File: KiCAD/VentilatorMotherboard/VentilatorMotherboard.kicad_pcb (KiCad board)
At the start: 2 copper layers, 139.7 x 151.1 mm, 31 parts

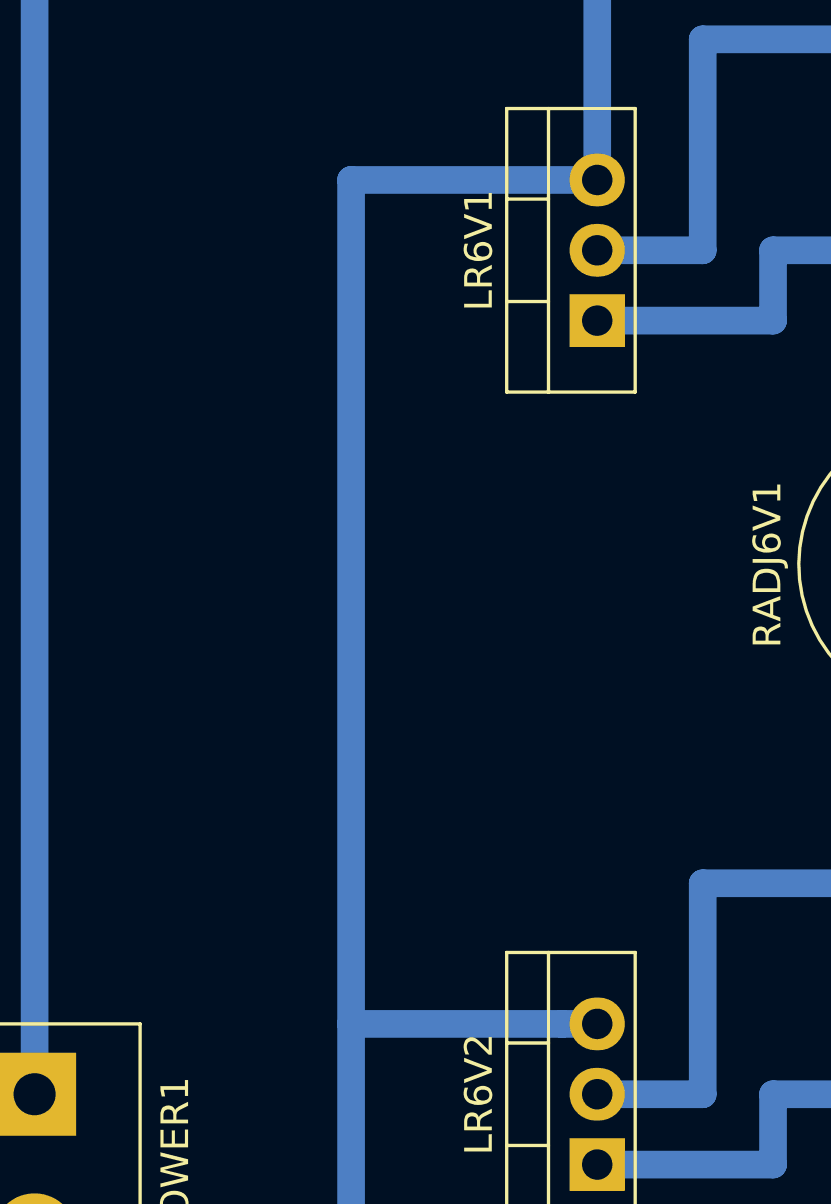
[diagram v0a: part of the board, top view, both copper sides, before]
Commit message: Add power switch to PCB; add some text annotations
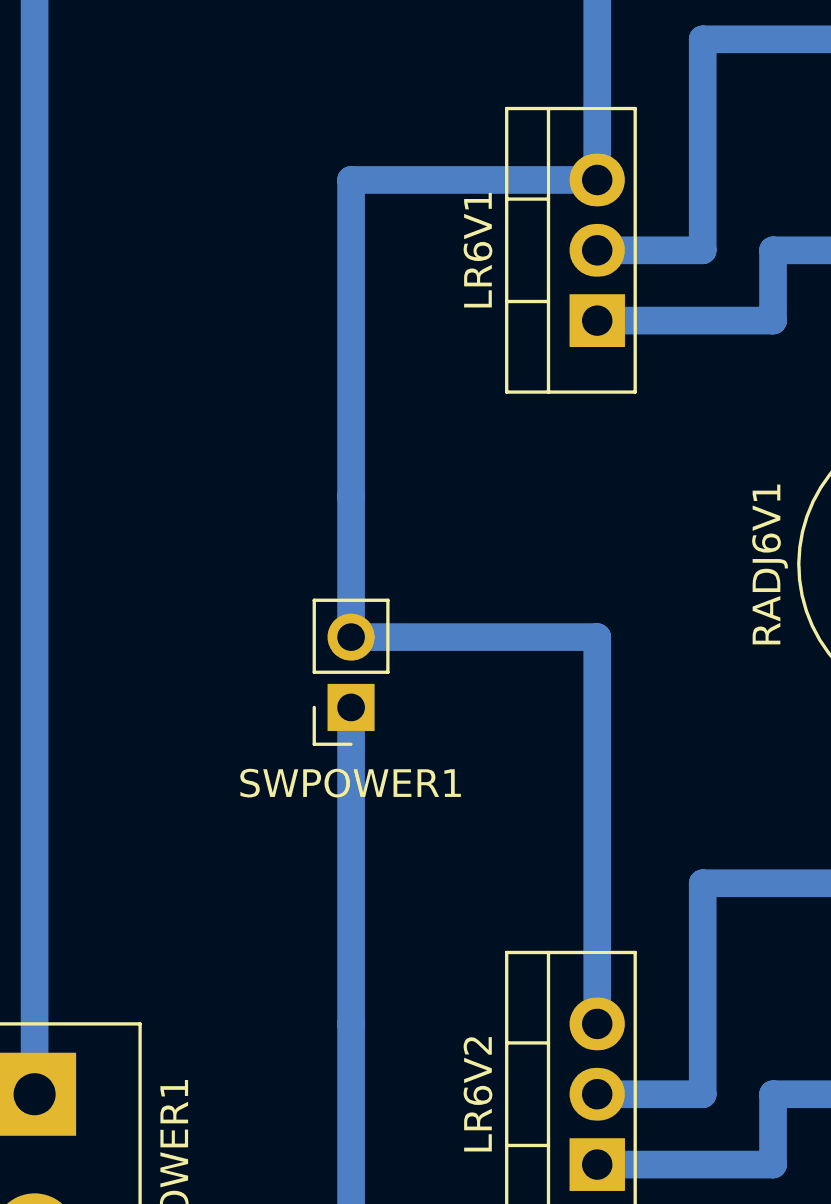
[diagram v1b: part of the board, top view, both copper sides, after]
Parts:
- added SWPOWER1: SW_SPST, Connector_PinSocket_2.54mm:PinSocket_1x02_P2.54mm_Vertical, F.Cu at (59.7, 59.7)
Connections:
- LR5V1 pad 1: Net-(JPOWER1-Pad2) -> Net-(LR5V1-Pad1)
- LR6V1 pad 3: Net-(JPOWER1-Pad2) -> Net-(LR5V1-Pad1)
- LR6V2 pad 3: Net-(JPOWER1-Pad2) -> Net-(LR5V1-Pad1)
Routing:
- net Net-(LR5V1-Pad1): track 0.00 -> 116.8 mm
- net Net-(JPOWER1-Pad2): track 135.9 -> 30.5 mm
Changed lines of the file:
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@@
     (thickness 1.6)
     (drawings 13)
-    (tracks 169)
+    (tracks 171)
     (zones 0)
-    (modules 31)
-    (nets 24)
+    (modules 32)
+    (nets 25)
   )
   (page A4)
@@
     (35 F.Paste user)
     (36 B.SilkS user)
-    (37 F.SilkS user hide)
+    (37 F.SilkS user)
     (38 B.Mask user)
     (39 F.Mask user)
@@
     (47 F.CrtYd user)
     (48 B.Fab user)
-    (49 F.Fab user hide)
+    (49 F.Fab user)
   )
   (setup
@@
     (solder_mask_min_width 0.25)
     (aux_axis_origin 0 0)
-    (visible_elements FFFFFF7F)
+    (visible_elements 7FFFFFFF)
     (pcbplotparams
       (layerselection 0x01000_ffffffff)
@@
   (net 22 "Net-(JPRESSURE2_46_1-Pad1)")
   (net 23 "Net-(CSPKCOUP1-Pad2)")
+  (net 24 "Net-(LR5V1-Pad1)")
   (net_class Default "This is the default net class."
     (clearance 0.2)
@@
     (uvia_drill 0.1)
     (add_net +5V)
+    (add_net /3V3)
     (add_net /6V1)
     (add_net /6V2)
@@
     (add_net /A4)
     (add_net /A5)
+    (add_net /A6)
+    (add_net /A7)
     (add_net /D10)
+    (add_net /D11)
+    (add_net /D12)
+    (add_net /D13)
+    (add_net /D2)
+    (add_net /D3)
     (add_net /D4)
     (add_net /D5)
+    (add_net /D6)
+    (add_net /D7)
+    (add_net /D8)
+    (add_net /D9)
+    (add_net /REF)
+    (add_net /RX0)
+    (add_net /TX1)
+    (add_net /VIN)
     (add_net GND)
+    (add_net "Net-(ARDUINOD12-Pad13)")
+    (add_net "Net-(ARDUINOD13-Pad13)")
     (add_net "Net-(CSPKCOUP1-Pad2)")
     (add_net "Net-(JPOWER1-Pad2)")
     (add_net "Net-(JPRESSURE1_13_1-Pad1)")
+    (add_net "Net-(JPRESSURE1_13_1-Pad2)")
     (add_net "Net-(JPRESSURE1_13_1-Pad3)")
     (add_net "Net-(JPRESSURE1_46_1-Pad1)")
+    (add_net "Net-(JPRESSURE1_46_1-Pad2)")
+    (add_net "Net-(JPRESSURE1_46_1-Pad3)")
     (add_net "Net-(JPRESSURE2_13_1-Pad1)")
+    (add_net "Net-(JPRESSURE2_13_1-Pad2)")
     (add_net "Net-(JPRESSURE2_13_1-Pad3)")
     (add_net "Net-(JPRESSURE2_46_1-Pad1)")
+    (add_net "Net-(JPRESSURE2_46_1-Pad2)")
+    (add_net "Net-(JPRESSURE2_46_1-Pad3)")
+    (add_net "Net-(LR5V1-Pad1)")
     (add_net "Net-(LR6V1-Pad1)")
     (add_net "Net-(LR6V2-Pad1)")
+    (add_net "Net-(RADJ6V1-Pad3)")
+    (add_net "Net-(RADJ6V2-Pad3)")
+  )
+  (module Connector_PinSocket_2.54mm:PinSocket_1x02_P2.54mm_Vertical (layer F.Cu)
+    (at 59.69 59.69 180)
+    (descr "Through hole straight socket strip, 1x02, 2.54mm pitch, single row (from Kicad 4.0.7), script generated")
+    (tags "Through hole socket strip THT 1x02 2.54mm single row")
+    (fp_text reference SWPOWER1 (at 0 -2.77) (layer F.SilkS)
+      (effects (font (size 1 1) (thickness 0.15)))
+    )
+    (fp_text value SW_SPST (at 0 5.31) (layer F.Fab)
+      (effects (font (size 1 1) (thickness 0.15)))
+    )
+    (fp_text user %R (at 0 1.27 90) (layer F.Fab)
+      (effects (font (size 1 1) (thickness 0.15)))
+    )
+    (fp_line (start -1.8 4.3) (end -1.8 -1.8) (layer F.CrtYd) (width 0.05))
+    (fp_line (start 1.75 4.3) (end -1.8 4.3) (layer F.CrtYd) (width 0.05))
+    (fp_line (start 1.75 -1.8) (end 1.75 4.3) (layer F.CrtYd) (width 0.05))
+    (fp_line (start -1.8 -1.8) (end 1.75 -1.8) (layer F.CrtYd) (width 0.05))
+    (fp_line (start 0 -1.33) (end 1.33 -1.33) (layer F.SilkS) (width 0.12))
+    (fp_line (start 1.33 -1.33) (end 1.33 0) (layer F.SilkS) (width 0.12))
+    (fp_line (start 1.33 1.27) (end 1.33 3.87) (layer F.SilkS) (width 0.12))
+    (fp_line (start -1.33 3.87) (end 1.33 3.87) (layer F.SilkS) (width 0.12))
+    (fp_line (start -1.33 1.27) (end -1.33 3.87) (layer F.SilkS) (width 0.12))
+    (fp_line (start -1.33 1.27) (end 1.33 1.27) (layer F.SilkS) (width 0.12))
+    (fp_line (start -1.27 3.81) (end -1.27 -1.27) (layer F.Fab) (width 0.1))
+    (fp_line (start 1.27 3.81) (end -1.27 3.81) (layer F.Fab) (width 0.1))
+    (fp_line (start 1.27 -0.635) (end 1.27 3.81) (layer F.Fab) (width 0.1))
+    (fp_line (start 0.635 -1.27) (end 1.27 -0.635) (layer F.Fab) (width 0.1))
+    (fp_line (start -1.27 -1.27) (end 0.635 -1.27) (layer F.Fab) (width 0.1))
+    (pad 2 thru_hole oval (at 0 2.54 180) (size 1.7 1.7) (drill 1) (layers *.Cu *.Mask)
+      (net 24 "Net-(LR5V1-Pad1)"))
+    (pad 1 thru_hole rect (at 0 0 180) (size 1.7 1.7) (drill 1) (layers *.Cu *.Mask)
+      (net 12 "Net-(JPOWER1-Pad2)"))
+    (model ${KISYS3DMOD}/Connector_PinSocket_2.54mm.3dshapes/PinSocket_1x02_P2.54mm_Vertical.wrl
+      (at (xyz 0 0 0))
+      (scale (xyz 1 1 1))
+      (rotate (xyz 0 0 0))
+    )
   )
   (module TerminalBlock:TerminalBlock_bornier-2_P5.08mm (layer F.Cu)
@@
     (fp_line (start -2.46 -3.15) (end -2.46 1.25) (layer F.Fab) (width 0.1))
     (pad 3 thru_hole oval (at 5.08 0 90) (size 1.905 2) (drill 1.1) (layers *.Cu *.Mask)
-      (net 12 "Net-(JPOWER1-Pad2)"))
+      (net 24 "Net-(LR5V1-Pad1)"))
     (pad 2 thru_hole oval (at 2.54 0 90) (size 1.905 2) (drill 1.1) (layers *.Cu *.Mask)
       (net 15 /6V2))
@@
     (fp_line (start -2.46 -3.15) (end -2.46 1.25) (layer F.Fab) (width 0.1))
     (pad 3 thru_hole oval (at 5.08 0 90) (size 1.905 2) (drill 1.1) (layers *.Cu *.Mask)
-      (net 12 "Net-(JPOWER1-Pad2)"))
+      (net 24 "Net-(LR5V1-Pad1)"))
     (pad 2 thru_hole oval (at 2.54 0 90) (size 1.905 2) (drill 1.1) (layers *.Cu *.Mask)
       (net 13 /6V1))
@@
       (net 1 GND))
     (pad 1 thru_hole rect (at 0 0 90) (size 1.905 2) (drill 1.1) (layers *.Cu *.Mask)
-      (net 12 "Net-(JPOWER1-Pad2)"))
+      (net 24 "Net-(LR5V1-Pad1)"))
     (model ${KISYS3DMOD}/Package_TO_SOT_THT.3dshapes/TO-220-3_Vertical.wrl
       (at (xyz 0 0 0))
@@
   (segment (start 148.59 113.03) (end 148.59 86.36) (width 1) (layer B.Cu) (net 11))
   (segment (start 177.8 113.03) (end 148.59 113.03) (width 1) (layer B.Cu) (net 11))
-  (segment (start 59.69 40.64) (end 68.58 40.64) (width 1) (layer B.Cu) (net 12))
-  (segment (start 68.58 40.64) (end 68.58 33.02) (width 1) (layer B.Cu) (net 12))
-  (segment (start 68.58 33.02) (end 113.03 33.02) (width 1) (layer B.Cu) (net 12))
-  (segment (start 113.03 33.02) (end 113.03 40.64) (width 1) (layer B.Cu) (net 12))
-  (segment (start 113.03 40.64) (end 121.92 40.64) (width 1) (layer B.Cu) (net 12))
-  (segment (start 59.69 40.64) (end 59.69 71.12) (width 1) (layer B.Cu) (net 12))
-  (segment (start 67.31 71.12) (end 68.58 71.12) (width 1) (layer B.Cu) (net 12))
-  (segment (start 59.69 71.12) (end 67.31 71.12) (width 1) (layer B.Cu) (net 12))
+  (segment (start 59.69 40.64) (end 68.58 40.64) (width 1) (layer B.Cu) (net 24))
+  (segment (start 68.58 40.64) (end 68.58 33.02) (width 1) (layer B.Cu) (net 24))
+  (segment (start 68.58 33.02) (end 113.03 33.02) (width 1) (layer B.Cu) (net 24))
+  (segment (start 113.03 33.02) (end 113.03 40.64) (width 1) (layer B.Cu) (net 24))
+  (segment (start 113.03 40.64) (end 121.92 40.64) (width 1) (layer B.Cu) (net 24))
   (segment (start 48.26 78.74) (end 59.69 78.74) (width 1) (layer B.Cu) (net 12))
   (segment (start 59.69 78.74) (end 59.69 71.12) (width 1) (layer B.Cu) (net 12))
+  (segment (start 59.69 71.12) (end 59.69 59.69) (width 1) (layer B.Cu) (net 12))
   (segment (start 68.58 43.18) (end 72.39 43.18) (width 1) (layer B.Cu) (net 13))
   (segment (start 72.39 43.18) (end 72.39 35.56) (width 1) (layer B.Cu) (net 13))
@@
   (segment (start 102.87 105.41) (end 102.87 104.14) (width 1) (layer B.Cu) (net 23))
   (segment (start 102.87 104.14) (end 97.79 104.14) (width 1) (layer B.Cu) (net 23))
+  (segment (start 59.69 52.07) (end 59.69 40.64) (width 1) (layer B.Cu) (net 24))
+  (segment (start 59.69 57.15) (end 59.69 52.07) (width 1) (layer B.Cu) (net 24))
+  (segment (start 59.69 57.15) (end 68.58 57.15) (width 1) (layer B.Cu) (net 24))
+  (segment (start 68.58 57.15) (end 68.58 71.12) (width 1) (layer B.Cu) (net 24))
 )
